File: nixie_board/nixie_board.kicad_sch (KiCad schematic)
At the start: 43 parts, among them J1 Conn_01x10_Pin, Q1 MMBTA42, Q10 MMBTA42, Q11 MMBTA42, Q2 MMBTA42, Q3 MMBTA42, Q4 MMBTA42, Q5 MMBTA42, Q6 MMBTA42, Q7 MMBTA42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

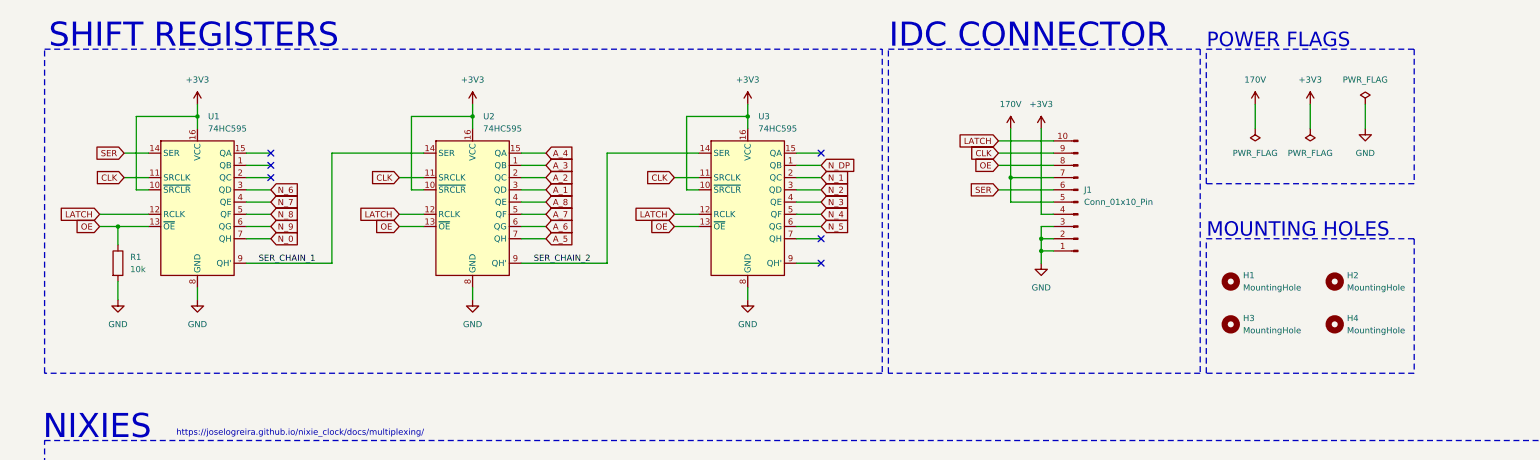
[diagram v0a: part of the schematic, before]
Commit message: Added vents to case
Added vents to the underside of the case to encourage airflow.
Also fixed some stupid design mistakes on the PCBs. This is the night
before EMTH btw.
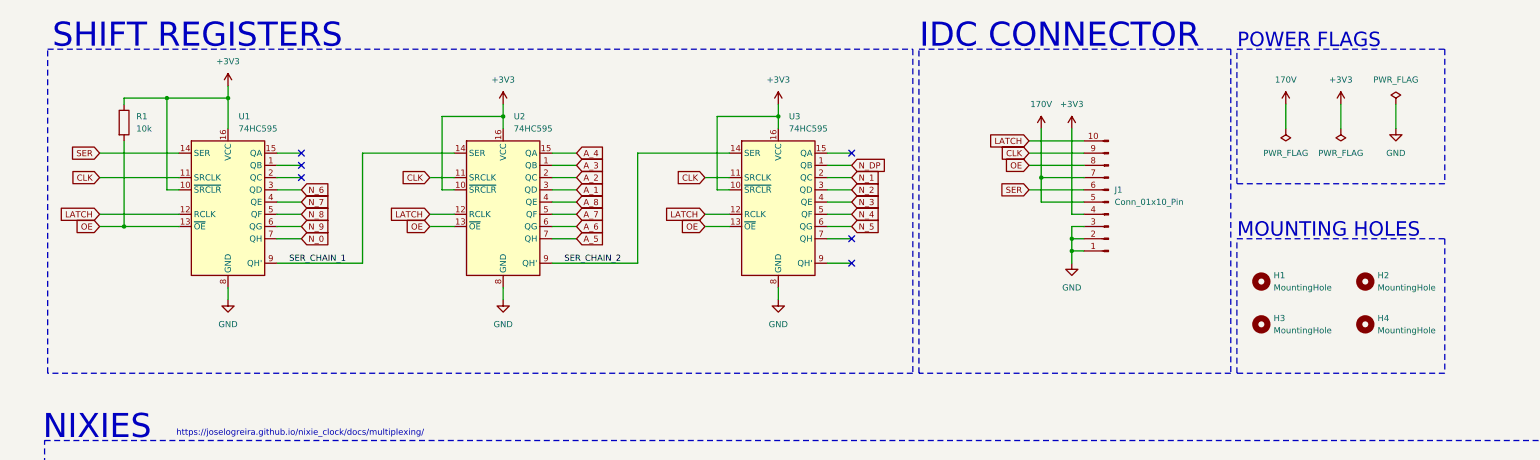
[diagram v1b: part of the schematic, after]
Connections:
- net +3V3: now also R1.1
- net GND: no longer R1.2
- net OE: now also R1.2; no longer R1.1
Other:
- moved on the sheet: H1, H2, H3, H4, J1, U1, U2, U3
